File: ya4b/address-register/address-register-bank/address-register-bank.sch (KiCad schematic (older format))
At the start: 99 parts, among them J1 Conn_01x38_Male, U1 GAL16V8, U10 74LS169, U11 74LS169, U12 74LS541, U13 74LS169, U14 74LS169, U15 74LS541, U16 74LS169, U17 74LS169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

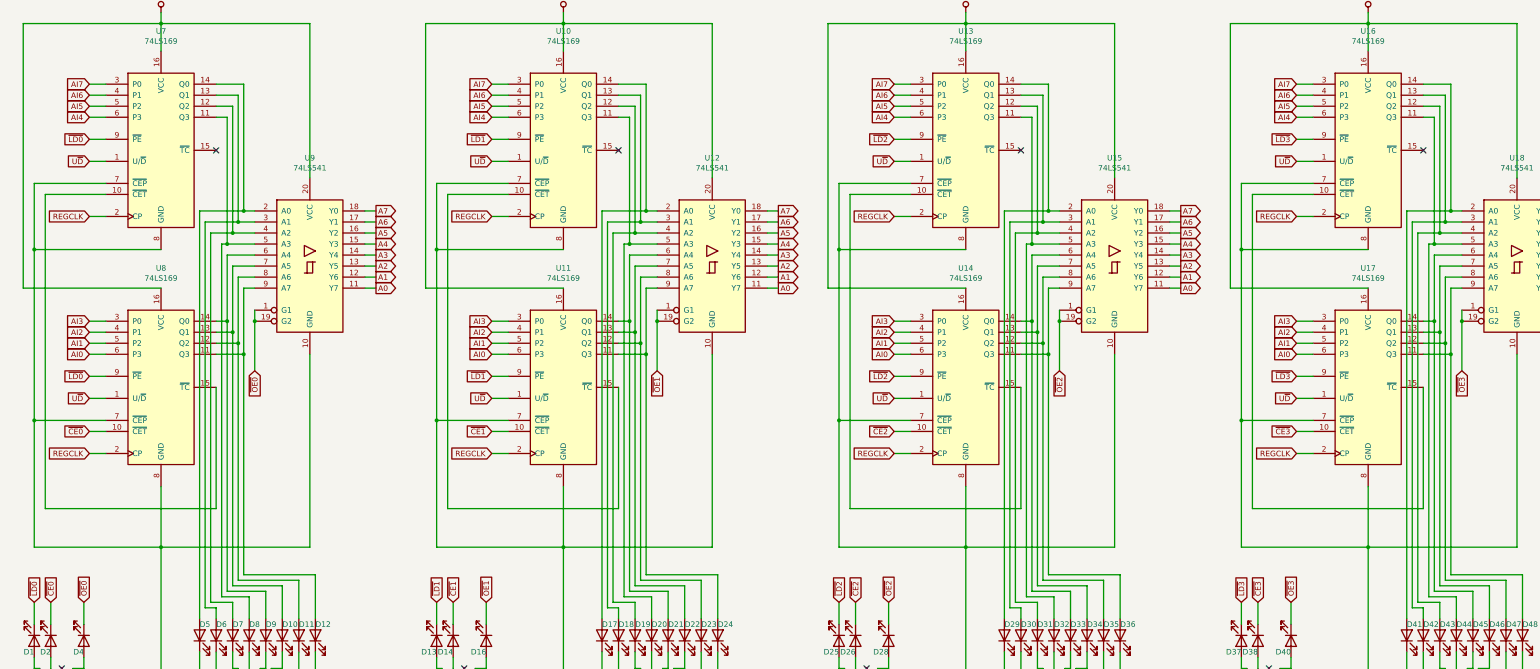
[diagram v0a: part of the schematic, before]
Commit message: Fixed PCB design files for address register bank
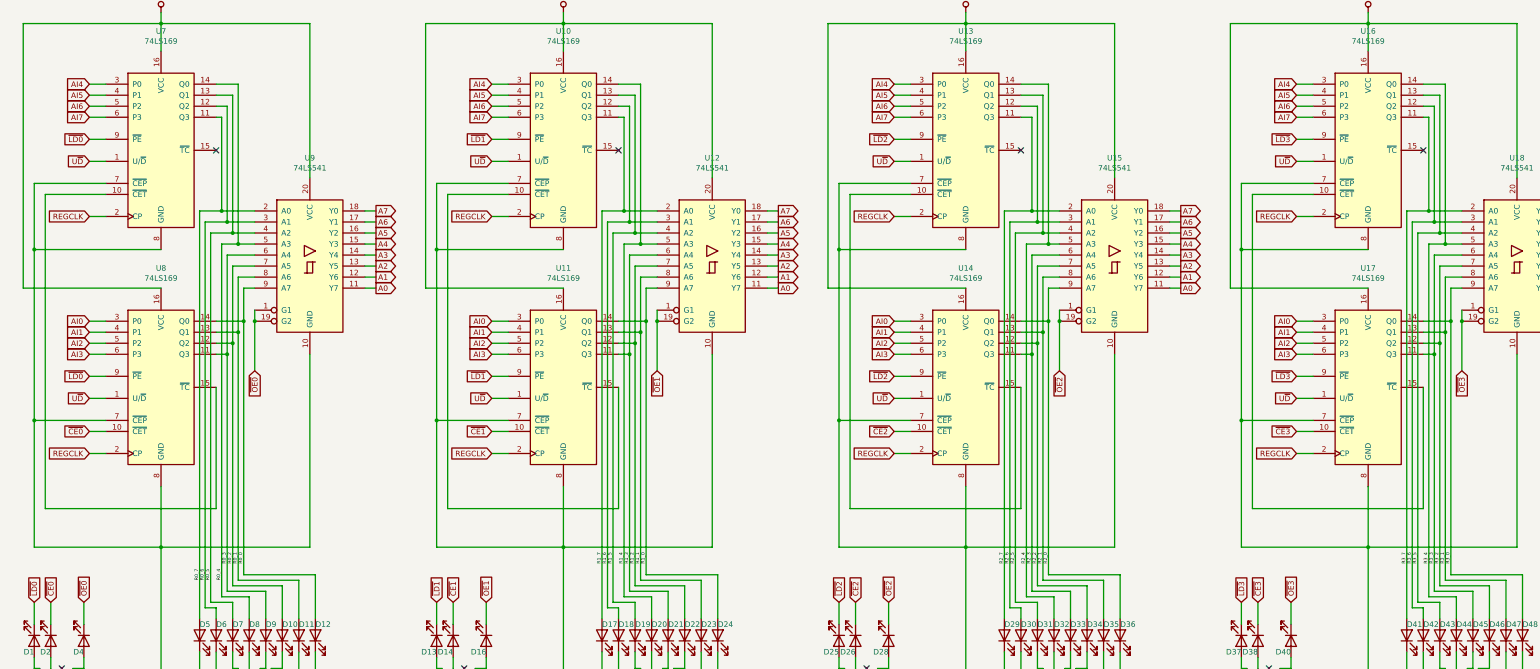
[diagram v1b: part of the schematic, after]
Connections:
- net AI0: now also U11.3 (P0), U14.3 (P0), U17.3 (P0), U8.3 (P0); no longer U11.6 (P3), U14.6 (P3), U17.6 (P3), U8.6 (P3)
- net AI1: now also U11.4 (P1), U14.4 (P1), U17.4 (P1), U8.4 (P1); no longer U11.5 (P2), U14.5 (P2), U17.5 (P2), U8.5 (P2)
- net AI2: now also U11.5 (P2), U14.5 (P2), U17.5 (P2), U8.5 (P2); no longer U11.4 (P1), U14.4 (P1), U17.4 (P1), U8.4 (P1)
- net AI3: now also U11.6 (P3), U14.6 (P3), U17.6 (P3), U8.6 (P3); no longer U11.3 (P0), U14.3 (P0), U17.3 (P0), U8.3 (P0)
- net AI4: now also U10.3 (P0), U13.3 (P0), U16.3 (P0), U7.3 (P0); no longer U10.6 (P3), U13.6 (P3), U16.6 (P3), U7.6 (P3)
- net AI5: now also U10.4 (P1), U13.4 (P1), U16.4 (P1), U7.4 (P1); no longer U10.5 (P2), U13.5 (P2), U16.5 (P2), U7.5 (P2)
- net AI6: now also U10.5 (P2), U13.5 (P2), U16.5 (P2), U7.5 (P2); no longer U10.4 (P1), U13.4 (P1), U16.4 (P1), U7.4 (P1)
- net AI7: now also U10.6 (P3), U13.6 (P3), U16.6 (P3), U7.6 (P3); no longer U10.3 (P0), U13.3 (P0), U16.3 (P0), U7.3 (P0)
- net R0_4: now reaches D8.2 (A), U9.5 (A3)
- net R0_4: now also U7.14 (Q0); no longer U7.11 (Q3)
- net R0_5: now reaches D7.2 (A), U9.4 (A2)
- net R0_5: now also U7.13 (Q1); no longer U7.12 (Q2)
- net R0_6: now reaches D6.2 (A), U9.3 (A1)
- net R0_6: now also U7.12 (Q2); no longer U7.13 (Q1)
- net R0_7: now reaches D5.2 (A), U9.2 (A0)
- net R0_7: now also U7.11 (Q3); no longer U7.14 (Q0)
- net R0_0: now reaches D12.2 (A), U9.9 (A7)
- net R0_0: now also U8.14 (Q0); no longer U8.11 (Q3)
- net R0_1: now reaches D11.2 (A), U9.8 (A6)
- net R0_1: now also U8.13 (Q1); no longer U8.12 (Q2)
- net R0_2: now reaches D10.2 (A), U9.7 (A5)
- net R0_2: now also U8.12 (Q2); no longer U8.13 (Q1)
- net R0_3: now reaches D9.2 (A), U9.6 (A4)
- net R0_3: now also U8.11 (Q3); no longer U8.14 (Q0)
- net R1_4: now reaches D20.2 (A), U12.5 (A3)
- net R1_4: now also U10.14 (Q0); no longer U10.11 (Q3)
- net R1_5: now reaches D19.2 (A), U12.4 (A2)
- net R1_5: now also U10.13 (Q1); no longer U10.12 (Q2)
- net R1_6: now reaches D18.2 (A), U12.3 (A1)
- net R1_6: now also U10.12 (Q2); no longer U10.13 (Q1)
- net R1_7: now reaches D17.2 (A), U12.2 (A0)
- net R1_7: now also U10.11 (Q3); no longer U10.14 (Q0)
- net R1_0: now reaches D24.2 (A), U12.9 (A7)
- net R1_0: now also U11.14 (Q0); no longer U11.11 (Q3)
- net R1_1: now reaches D23.2 (A), U12.8 (A6)
- net R1_1: now also U11.13 (Q1); no longer U11.12 (Q2)
- net R1_2: now reaches D22.2 (A), U12.7 (A5)
- net R1_2: now also U11.12 (Q2); no longer U11.13 (Q1)
- net R1_3: now reaches D21.2 (A), U12.6 (A4)
- net R1_3: now also U11.11 (Q3); no longer U11.14 (Q0)
- net R2_4: now reaches D32.2 (A), U15.5 (A3)
- net R2_4: now also U13.14 (Q0); no longer U13.11 (Q3)
- net R2_5: now reaches D31.2 (A), U15.4 (A2)
- net R2_5: now also U13.13 (Q1); no longer U13.12 (Q2)
- net R2_6: now reaches D30.2 (A), U15.3 (A1)
- net R2_6: now also U13.12 (Q2); no longer U13.13 (Q1)
- net R2_7: now reaches D29.2 (A), U15.2 (A0)
- net R2_7: now also U13.11 (Q3); no longer U13.14 (Q0)
- net R2_0: now reaches D36.2 (A), U15.9 (A7)
- net R2_0: now also U14.14 (Q0); no longer U14.11 (Q3)
- net R2_1: now reaches D35.2 (A), U15.8 (A6)
- net R2_1: now also U14.13 (Q1); no longer U14.12 (Q2)
- net R2_2: now reaches D34.2 (A), U15.7 (A5)
- net R2_2: now also U14.12 (Q2); no longer U14.13 (Q1)
- net R2_3: now reaches D33.2 (A), U15.6 (A4)
- net R2_3: now also U14.11 (Q3); no longer U14.14 (Q0)
- net R3_4: now reaches D44.2 (A), U18.5 (A3)
- net R3_4: now also U16.14 (Q0); no longer U16.11 (Q3)
- net R3_5: now reaches D43.2 (A), U18.4 (A2)
- net R3_5: now also U16.13 (Q1); no longer U16.12 (Q2)
- net R3_6: now reaches D42.2 (A), U18.3 (A1)
- net R3_6: now also U16.12 (Q2); no longer U16.13 (Q1)
- net R3_7: now reaches D41.2 (A), U18.2 (A0)
- net R3_7: now also U16.11 (Q3); no longer U16.14 (Q0)
- net R3_0: now reaches D48.2 (A), U18.9 (A7)
- net R3_0: now also U17.14 (Q0); no longer U17.11 (Q3)
- net R3_1: now reaches D47.2 (A), U18.8 (A6)
- net R3_1: now also U17.13 (Q1); no longer U17.12 (Q2)
- net R3_2: now reaches D46.2 (A), U18.7 (A5)
- net R3_2: now also U17.12 (Q2); no longer U17.13 (Q1)
- net R3_3: now reaches D45.2 (A), U18.6 (A4)
- net R3_3: now also U17.11 (Q3); no longer U17.14 (Q0)
